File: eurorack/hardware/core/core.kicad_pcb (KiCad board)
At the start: 2 copper layers, 43 parts, among them J1 ConnNW, J2 ConnSW, J3 ConnNE, J4 ConnSE, J5 Power, J6 SWD, SW1 Reset, SW2 Boot0, U1 STM32F427VGT6, U2 TLV320AIC23BPW, U3 LM1117F-3.3, Y1 Crystal

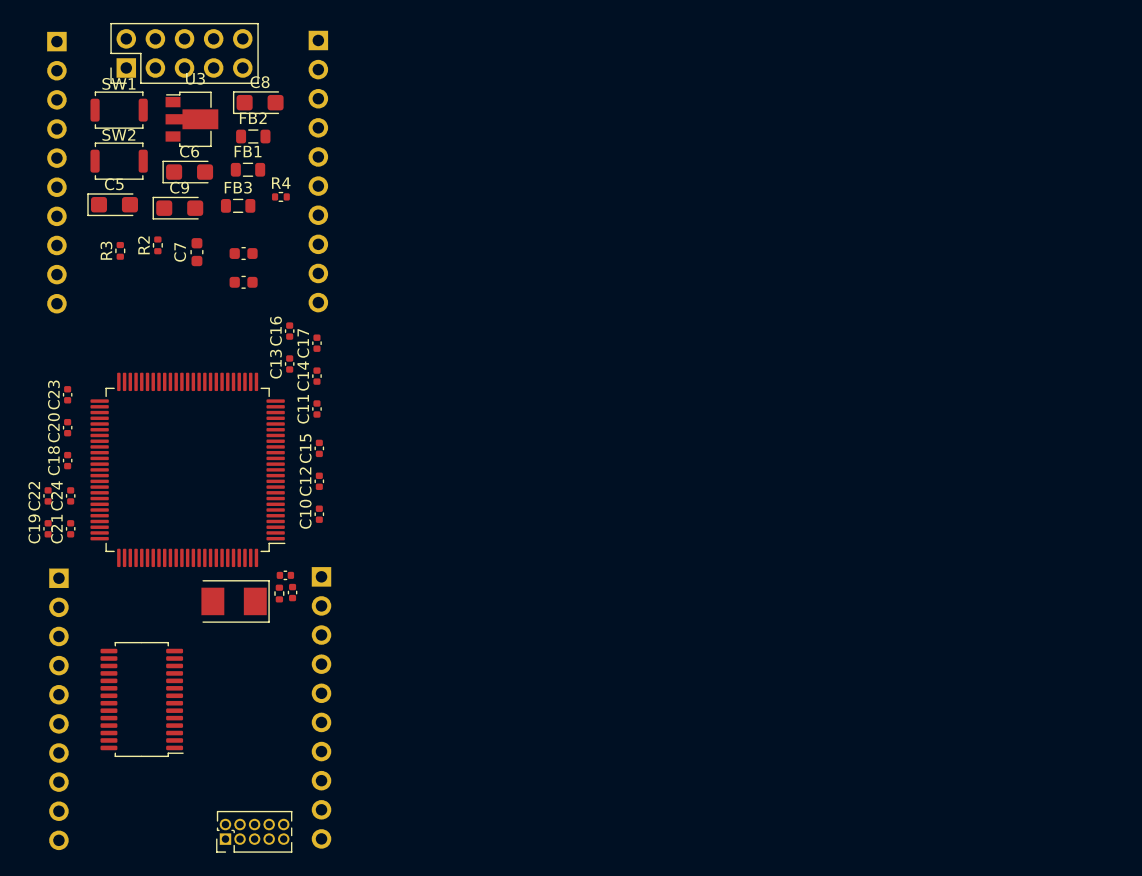
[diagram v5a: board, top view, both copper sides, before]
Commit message: Fit the PCB within 2 HP
Signed-off-by: Petr Horacek <hrck@protonmail.com>
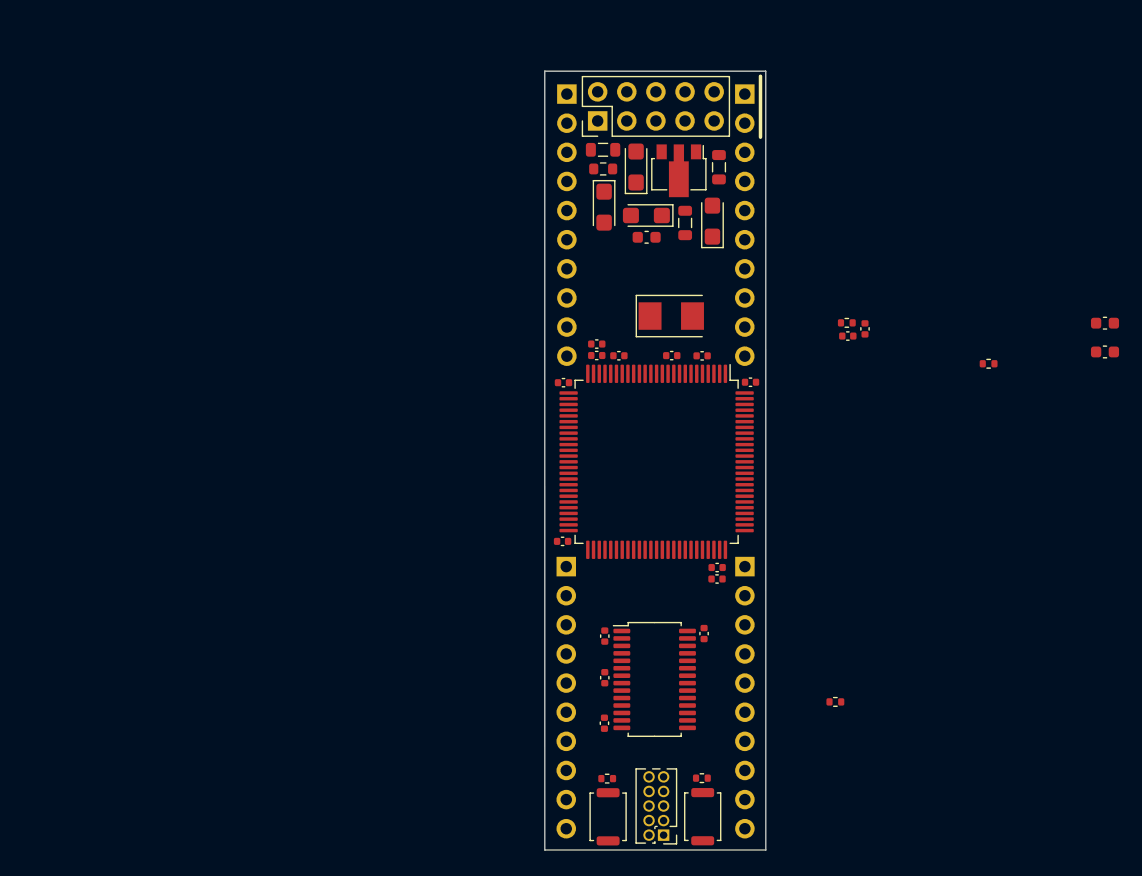
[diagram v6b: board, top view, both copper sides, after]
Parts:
- removed C24: 100n, Capacitor_SMD:C_0402_1005Metric
- added R5: 2k2, Resistor_SMD:R_0402_1005Metric, F.Cu at (192.9, 47.6)
- added R6: 2k2, Resistor_SMD:R_0402_1005Metric, F.Cu at (179.5, 77.1)
- R4: footprint Resistor_SMD:R_0402_1005Metric -> Resistor_SMD:R_0603_1608Metric
- moved SW1 79.9 mm to (168.0, 87.1), turned to 90 degrees
- moved C3 75.4 mm to (203.1, 44.1)
- moved C4 75.4 mm to (203.1, 46.6)
- moved SW2 71.3 mm to (159.7, 87.1), turned to 270 degrees
- moved R2 66.4 mm to (167.9, 83.8), turned to 0 degrees
- moved R3 62.6 mm to (159.6, 83.8), turned to 180 degrees
- moved C19 57.9 mm to (168.1, 71.2)
- moved C2 54.9 mm to (182.1, 44.6), turned to 270 degrees
- moved R1 54.8 mm to (180.5, 44.1), turned to 180 degrees
- moved C1 53.3 mm to (180.6, 45.2), turned to 0 degrees
- moved C23 52.9 mm to (159.4, 75.0)
- moved C22 52.4 mm to (159.4, 79.0)
- moved C18 49.3 mm to (159.4, 71.4), turned to 270 degrees
- moved C21 48.6 mm to (158.7, 45.9), turned to 180 degrees
- moved C20 46.6 mm to (158.7, 46.9), turned to 180 degrees
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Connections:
- J6 pad 1: Net-(J6-Pad1) -> +3V3
- J6 pad 3: Net-(J6-Pad3) -> GND
- J6 pad 5: Net-(J6-Pad5) -> GND
- J6 pad 9: Net-(J6-Pad9) -> GND
- U2 pad 1: Net-(U2-Pad1) -> +3V3
- U2 pad 11: Net-(U2-Pad11) -> GND
- U2 pad 14: Net-(U2-Pad14) -> +3.3VA
- U2 pad 15: Net-(U2-Pad15) -> GND
- U2 pad 21: Net-(U2-Pad21) -> GND
- U2 pad 22: Net-(U2-Pad22) -> GND
- U2 pad 27: Net-(U2-Pad27) -> +3V3
- U2 pad 28: Net-(U2-Pad28) -> GND
- U2 pad 8: Net-(U2-Pad8) -> +3.3VA
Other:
- board outline added: 19.3 x 67.9 mm

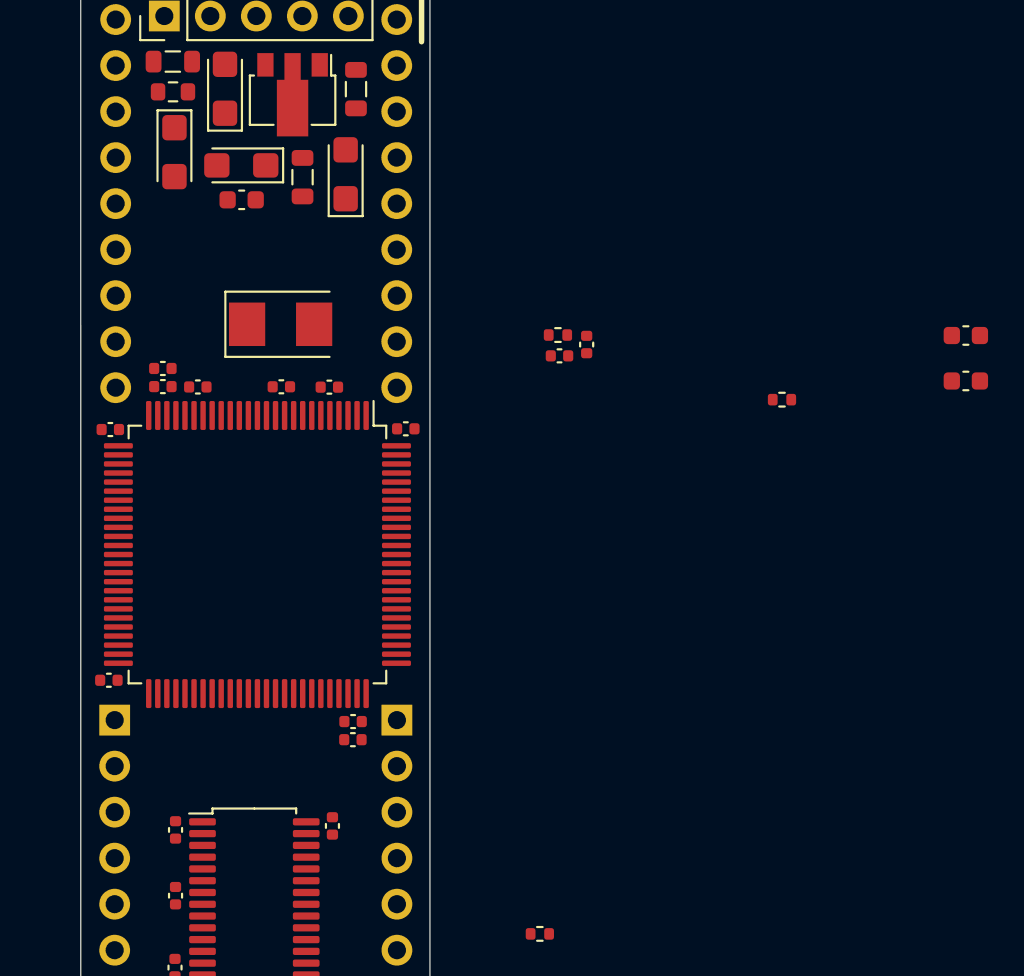
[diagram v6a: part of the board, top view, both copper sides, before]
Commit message: Add -10v reference voltage
Signed-off-by: Petr Horacek <hrck@protonmail.com>
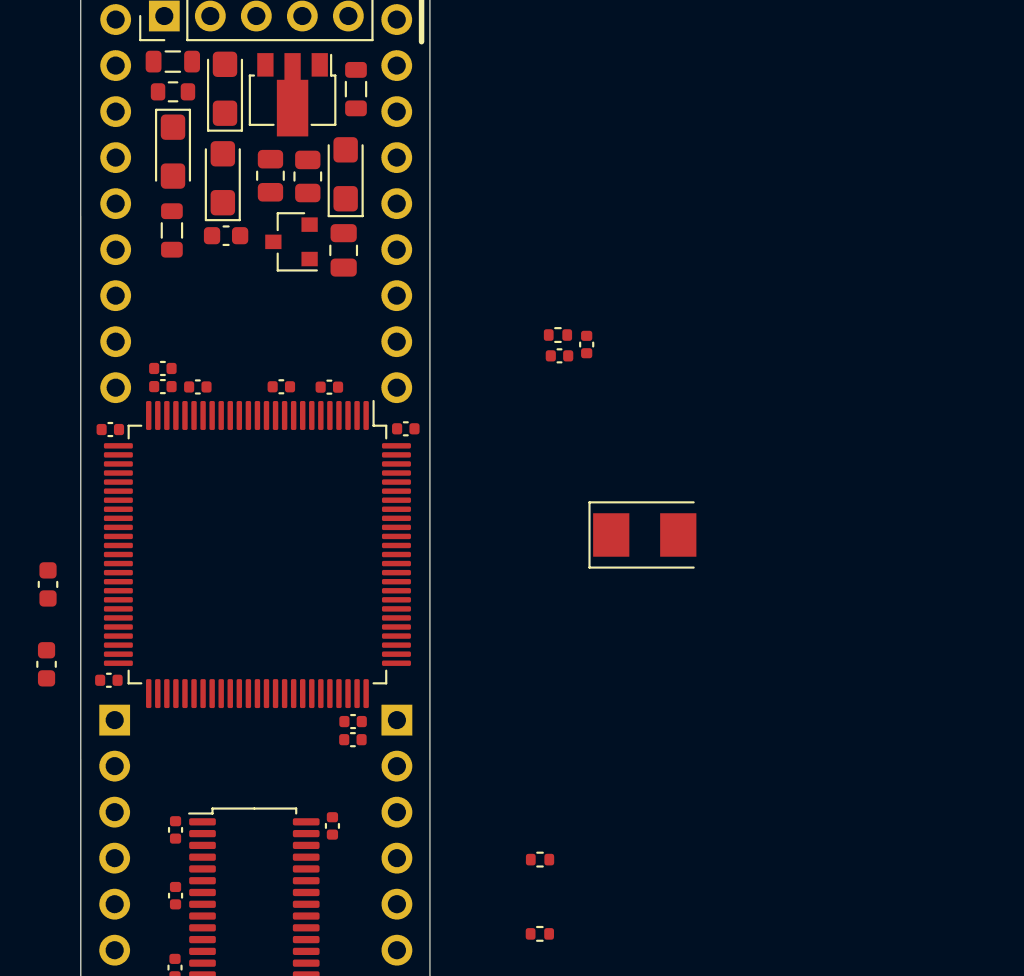
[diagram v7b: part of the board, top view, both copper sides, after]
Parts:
- added C24: 100n, Capacitor_SMD:C_0805_2012Metric, F.Cu at (168.7, 39.4)
- added R7: 1k, Resistor_SMD:R_0805_2012Metric, F.Cu at (164.7, 35.3)
- added R8: 1k, Resistor_SMD:R_0805_2012Metric, F.Cu at (166.7, 35.3)
- added U4: LM4040C10IDBZR, Package_TO_SOT_SMD:SOT-23, F.Cu at (165.8, 38.9)
- moved C3 53.9 mm to (152.3, 62.2), turned to 270 degrees
- moved C4 51.9 mm to (152.4, 57.8), turned to 90 degrees
- moved R5 28.7 mm to (179.6, 73.0)
- moved Y1 23.2 mm to (185.3, 55.1)
- moved FB3 7.79 mm to (159.2, 38.3)
- moved C7 2.16 mm to (162.2, 38.6), turned to 0 degrees
- moved C6 1.24 mm to (162.0, 35.4), turned to 90 degrees
- moved C8 0.09 mm to (159.3, 33.9)

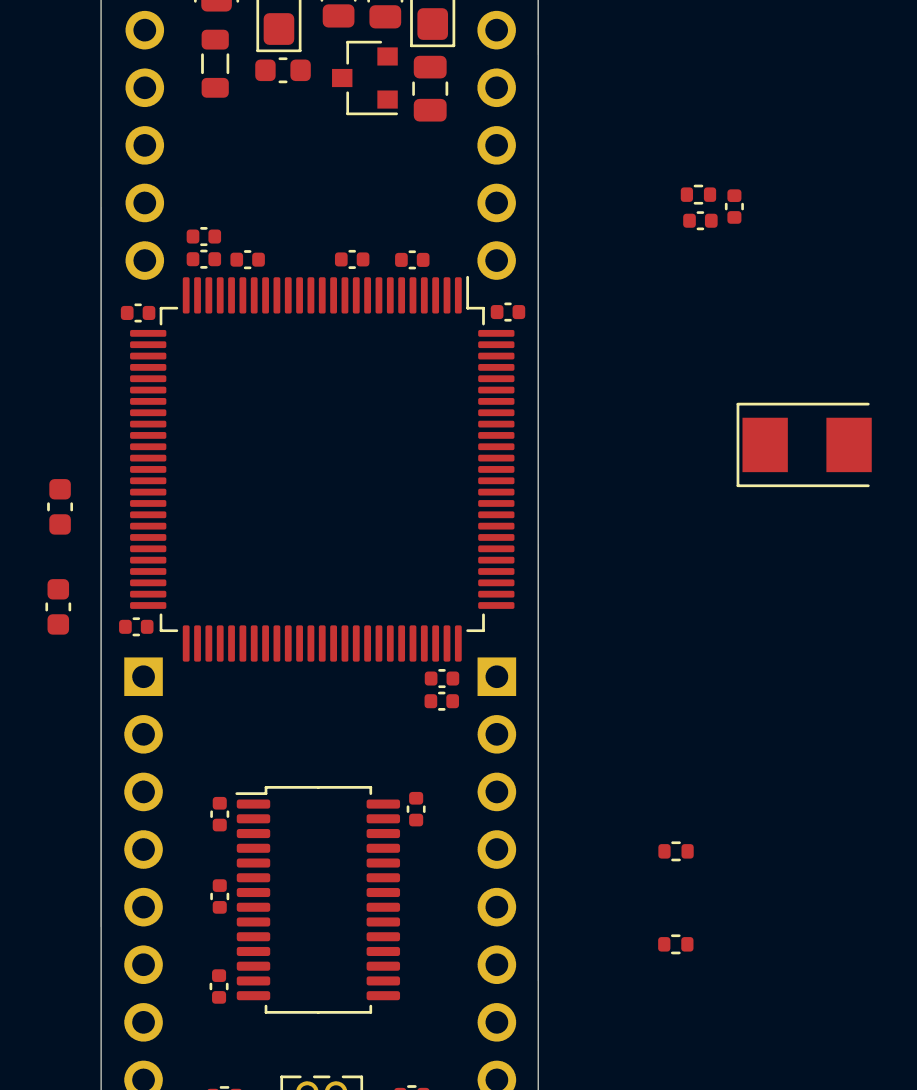
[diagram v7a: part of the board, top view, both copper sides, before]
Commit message: Connect DAC and JTAG
Signed-off-by: Petr Horacek <hrck@protonmail.com>
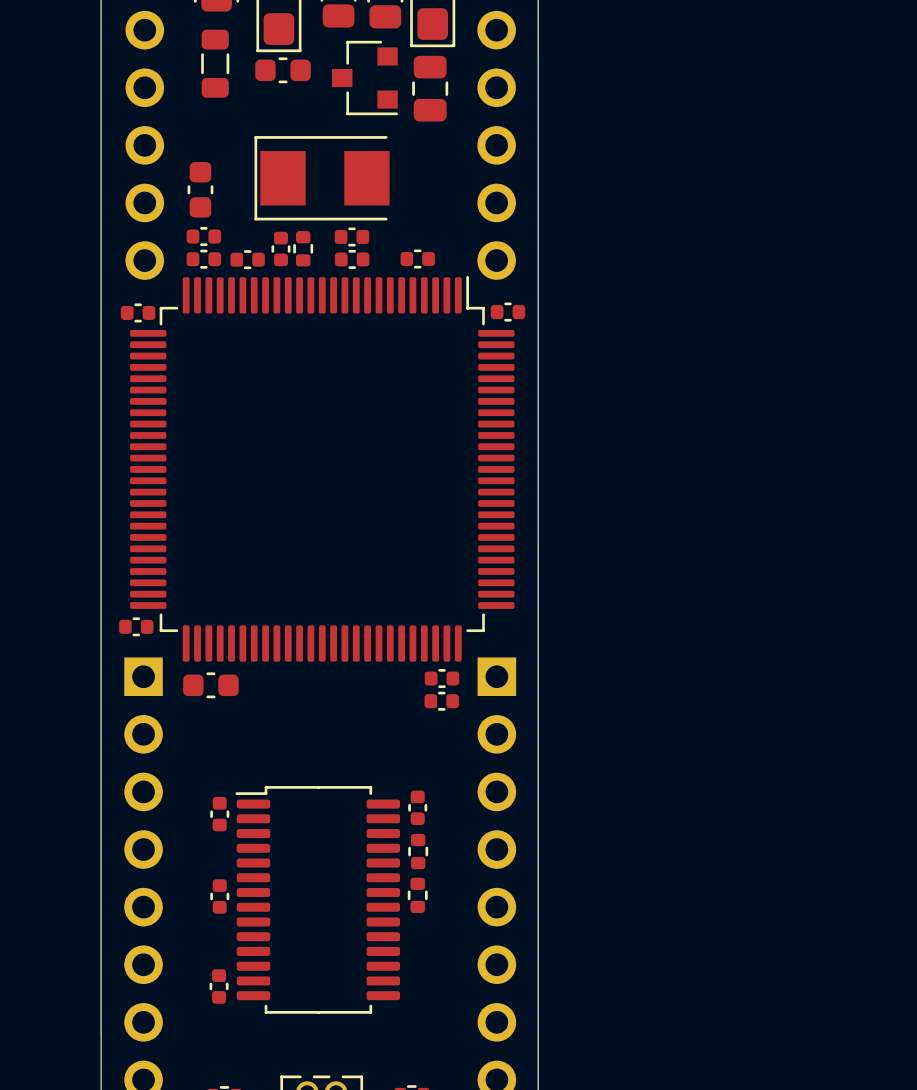
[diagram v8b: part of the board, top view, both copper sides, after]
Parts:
- moved Y1 24.3 mm to (164.1, 43.3)
- moved C1 18.5 mm to (162.1, 46.5), turned to 270 degrees
- moved R1 17.6 mm to (163.1, 46.4), turned to 90 degrees
- moved C2 16.9 mm to (165.3, 45.9), turned to 0 degrees
- moved C4 15.3 mm to (158.6, 43.8)
- moved R6 12.1 mm to (168.2, 73.0), turned to 270 degrees
- moved R5 11.6 mm to (168.2, 75.0), turned to 90 degrees
- moved C3 7.57 mm to (159.0, 65.7), turned to 0 degrees
- moved C17 0.24 mm to (168.2, 46.9)
- moved C19 0.09 mm to (168.2, 71.1)
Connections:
- J6 pad 10: Net-(J6-Pad10) -> NRST
- J6 pad 2: Net-(J6-Pad2) -> JTMS
- J6 pad 4: Net-(J6-Pad4) -> JTCK
- J6 pad 6: Net-(J6-Pad6) -> JTDO
- J6 pad 8: Net-(J6-Pad8) -> JTDI
- R5 pad 2: Net-(R5-Pad2) -> I2C_SDA
- R6 pad 2: Net-(R6-Pad2) -> I2C_SCL
- U1 pad 51: Net-(U1-Pad51) -> I2S_WS
- U1 pad 52: Net-(U1-Pad52) -> I2S_CK
- U1 pad 53: Net-(U1-Pad53) -> I2S_DIN
- U1 pad 54: Net-(U1-Pad54) -> I2S_DOUT
- U1 pad 63: Net-(U1-Pad63) -> I2S_MCK
- U1 pad 66: Net-(U1-Pad66) -> I2C_SDA
- U1 pad 67: Net-(U1-Pad67) -> I2C_SCL
- U1 pad 72: Net-(U1-Pad72) -> JTMS
- U1 pad 76: Net-(U1-Pad76) -> JTCK
- U1 pad 77: Net-(U1-Pad77) -> JTDI
- U1 pad 89: Net-(U1-Pad89) -> JTDO
- U2 pad 23: Net-(R5-Pad2) -> I2C_SDA
- U2 pad 24: Net-(R6-Pad2) -> I2C_SCL
- U2 pad 25: Net-(U2-Pad25) -> I2S_MCK
- U2 pad 3: Net-(U2-Pad3) -> I2S_CK
- U2 pad 4: Net-(U2-Pad4) -> I2S_DIN
- U2 pad 5: Net-(U2-Pad5) -> I2S_WS
- U2 pad 6: Net-(U2-Pad6) -> I2S_DOUT
- U2 pad 7: Net-(U2-Pad7) -> I2S_WS
